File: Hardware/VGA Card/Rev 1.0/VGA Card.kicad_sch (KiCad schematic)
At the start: 25 parts, among them J1 Conn_02x08_Odd_Even, J2 6502 Card Edge, J3 DE15_Receptacle_HighDensity_M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, Q1 BSS138, U1 TXS0108EPW, U2 74HC138, U3 TXS0108EPW, U4 Raspberry Pi Pico

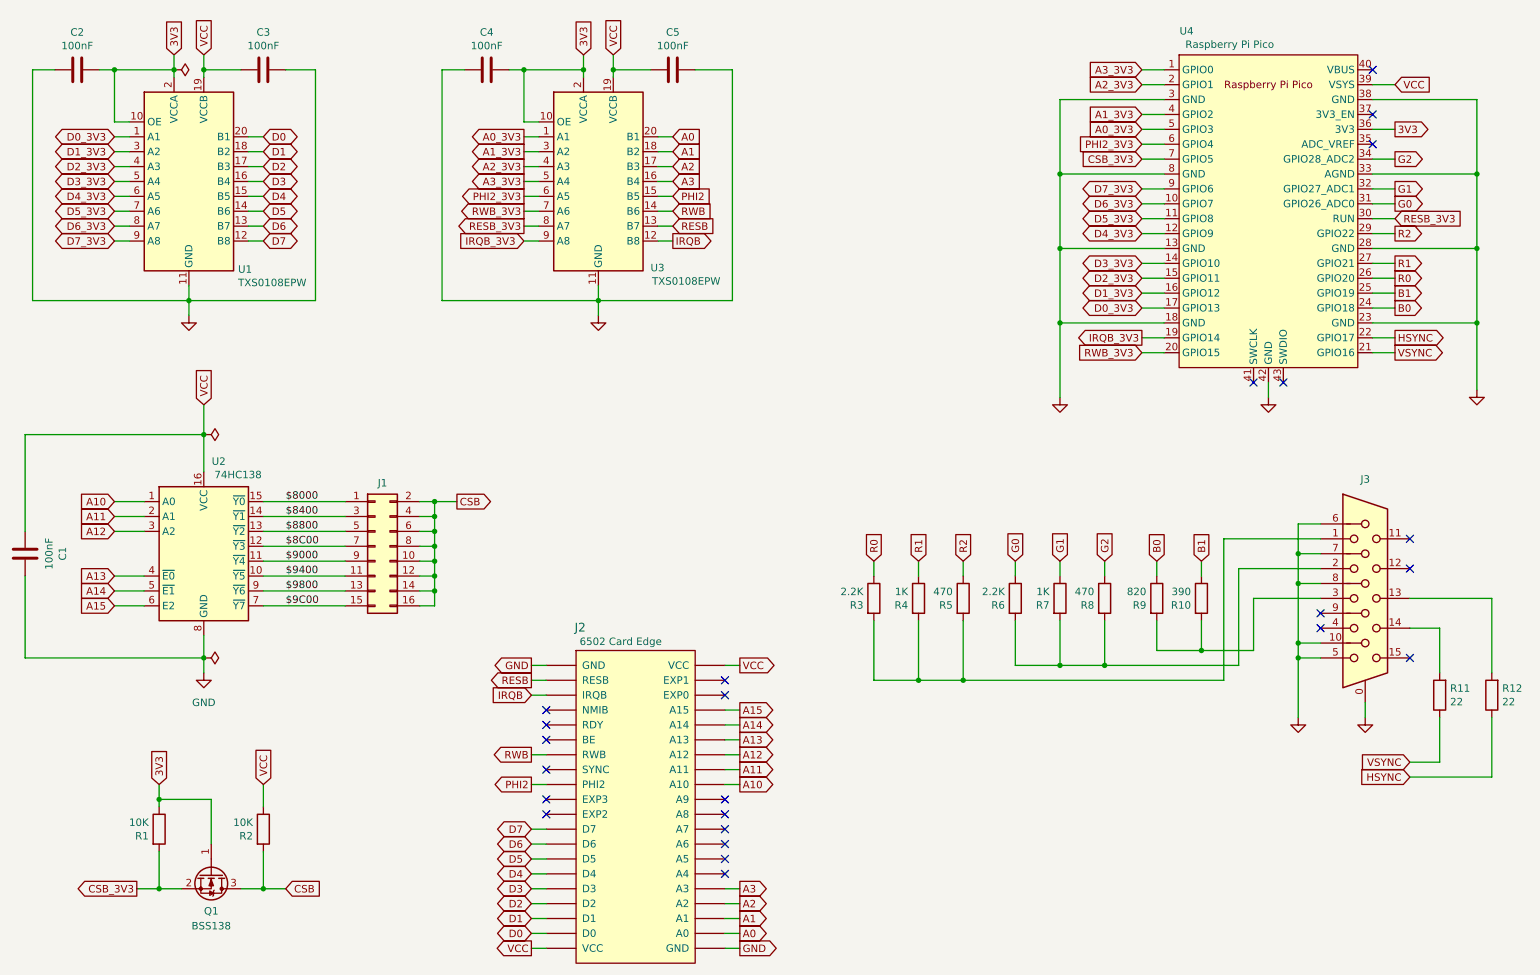
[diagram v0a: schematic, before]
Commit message: Redesign VGA card based on Pico9918A
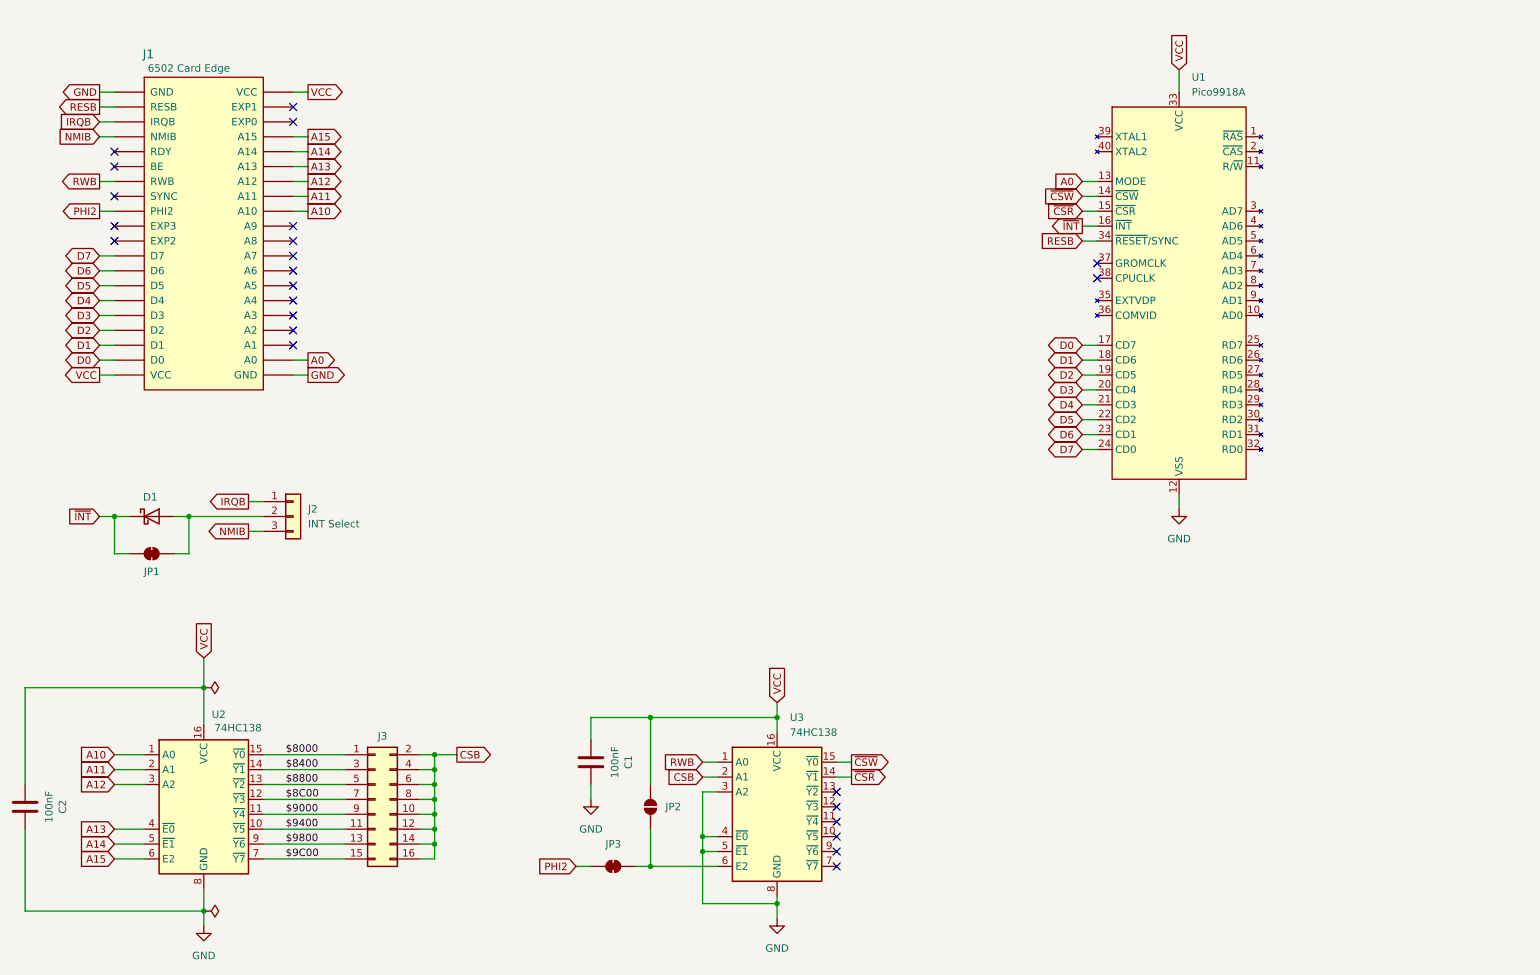
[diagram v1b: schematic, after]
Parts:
- removed C2, C3, C4, C5: 100nF, Capacitor_SMD:C_0805_2012Metric, symbol Device:C
- removed J3: DE15_Receptacle_HighDensity_MountingHoles, Connector_Dsub:DSUB-15-HD_Female_Horizontal_P2.29x1.98mm_EdgePinOffset3.03mm_Housed_MountingHolesOffset4.94mm, symbol Connector:DE15_Receptacle_HighDensity_MountingHoles
- removed Q1: BSS138, Package_TO_SOT_SMD:SOT-23, symbol Transistor_FET:BSS138
- removed R1, R2: 10K, Resistor_SMD:R_0805_2012Metric, symbol Device:R
- removed R10: 390, Resistor_SMD:R_0805_2012Metric, symbol Device:R
- removed R11, R12: 22, Resistor_SMD:R_0805_2012Metric, symbol Device:R
- removed R3, R6: 2.2K, Resistor_SMD:R_0805_2012Metric, symbol Device:R
- removed R4, R7: 1K, Resistor_SMD:R_0805_2012Metric, symbol Device:R
- removed R5, R8: 470, Resistor_SMD:R_0805_2012Metric, symbol Device:R
- removed R9: 820, Resistor_SMD:R_0805_2012Metric, symbol Device:R
- removed U1, U3: TXS0108EPW, Package_SO:TSSOP-20_4.4x6.5mm_P0.65mm, symbol Logic_LevelTranslator:TXS0108EPW
- removed U4: Raspberry Pi Pico, 6502 Parts:Raspberry Pi Pico, symbol 6502 Parts:Raspberry Pi Pico
- added C1: 100nF, Capacitor_SMD:C_0805_2012Metric, symbol Device:C
- added D1: D_Schottky, Diode_THT:D_DO-35_SOD27_P7.62mm_Horizontal, symbol Device:D_Schottky
- added J2: INT Select, Connector_PinHeader_2.54mm:PinHeader_1x03_P2.54mm_Vertical, symbol Connector_Generic:Conn_01x03
- added JP1, JP3: SolderJumper_2_Bridged, Jumper:SolderJumper-2_P1.3mm_Bridged_RoundedPad1.0x1.5mm, symbol Jumper:SolderJumper_2_Bridged
- added JP2: SolderJumper_2_Open, Jumper:SolderJumper-2_P1.3mm_Open_RoundedPad1.0x1.5mm, symbol Jumper:SolderJumper_2_Open
- added U1: Pico9918A, Package_DIP:DIP-40_W15.24mm_LongPads, symbol 6502 Parts:Pico9918A
- added U3: 74HC138, Package_SO:SOIC-16_3.9x9.9mm_P1.27mm, symbol 74xx:74HC138
- renumbered C1 to C2, J2 to J1, J1 to J3
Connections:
- net A0: now also U1.13 (MODE)
- net CSB: now also U3.2 (A1)
- net D0: now also U1.17 (CD7)
- net D1: now also U1.18 (CD6)
- net D2: now also U1.19 (CD5)
- net D3: now also U1.20 (CD4)
- net D4: now also U1.21 (CD3)
- net D5: now also U1.22 (CD2)
- net D6: now also U1.23 (CD1)
- net D7: now also U1.24 (CD0)
- net GND: now also C1.2, U1.12 (VSS), U3.3 (A2), U3.4 (~{E0}), U3.5 (~{E1}), U3.8 (GND)
- net IRQB: now also J2.1 (Pin_1)
- net PHI2: now also JP3.2 (B)
- net RESB: now also U1.34 (~{RESET}/SYNC)
- net RWB: now also U3.1 (A0)
- net VCC: now also C1.1, JP2.1 (A), U1.33 (VCC), U3.16 (VCC)
- net NMIB: now reaches J1.NMIB
- net NMIB: now also J2.3 (Pin_3)
- net A1: no longer names the net of J1.A1
- net A2: no longer names the net of J1.A2
- net A3: no longer names the net of J1.A3
- new net: D1.2 (A), J2.2 (Pin_2), JP1.2 (B)
- new net: JP2.2 (B), JP3.1 (A), U3.6 (E2)
- new net ~{CSR}: U1.15 (~{CSR}), U3.14 (~{Y1})
- new net ~{CSW}: U1.14 (~{CSW}), U3.15 (~{Y0})
- new net ~{INT}: D1.1 (K), JP1.1 (A), U1.16 (~{INT})
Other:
- moved on the sheet: C2, J1, J3, U2

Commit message: Fixes for production
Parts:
- U1: now left out of the parts list
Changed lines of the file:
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@@
 		(unit 1)
 		(exclude_from_sim no)
-		(in_bom yes)
+		(in_bom no)
 		(on_board yes)
 		(dnp no)

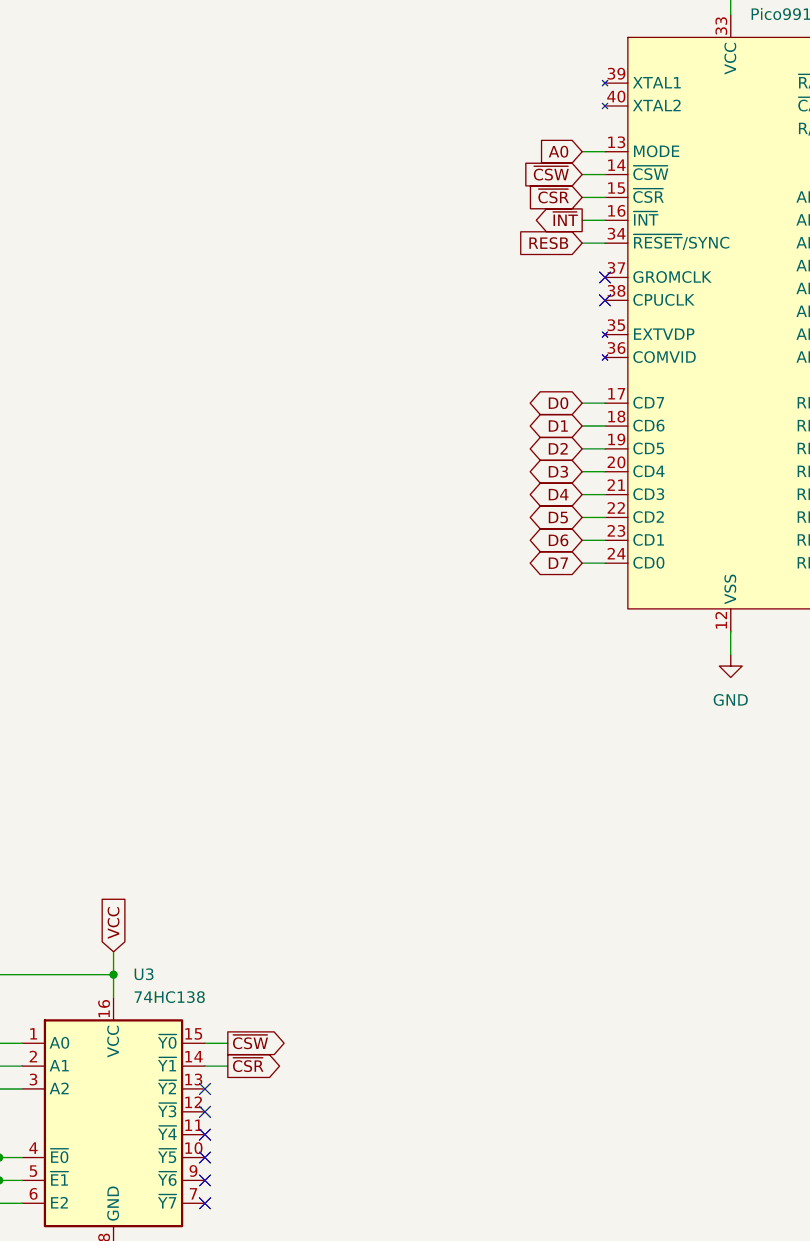
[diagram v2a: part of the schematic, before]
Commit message: Update schematics for pin naming consistency
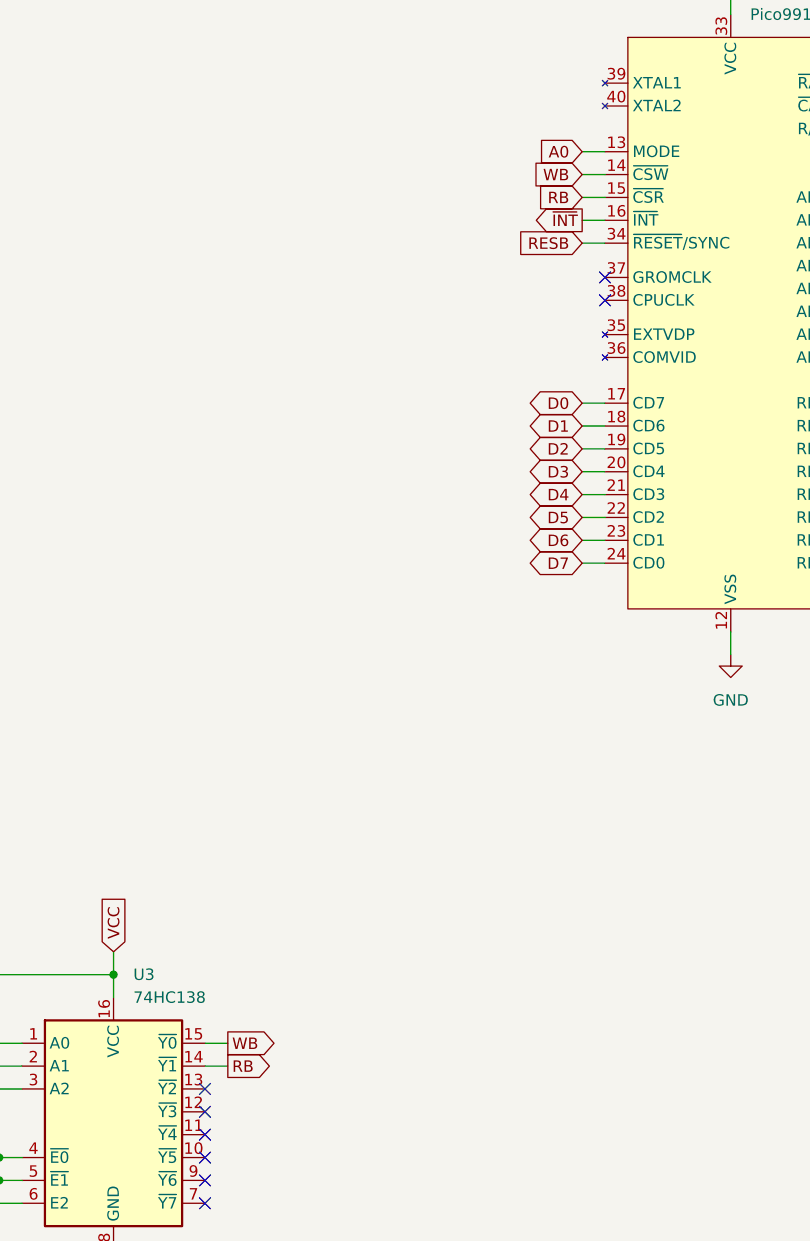
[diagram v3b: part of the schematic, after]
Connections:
- net ~{CSR} renamed RB
- net ~{CSW} renamed WB
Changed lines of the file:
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@@
 		)
 	)
-	(global_label "~{CSW}"
+	(global_label "WB"
 		(shape input)
 		(at 204.47 52.07 180)
@@
 		)
 		(property "Intersheetrefs" "${INTERSHEET_REFS}"
-			(at 197.5539 52.07 0)
+			(at 198.7634 52.07 0)
 			(effects
 				(font
@@
 		)
 	)
-	(global_label "~{CSW}"
+	(global_label "WB"
 		(shape output)
 		(at 165.1 148.59 0)
@@
 		)
 		(property "Intersheetrefs" "${INTERSHEET_REFS}"
-			(at 172.0161 148.59 0)
+			(at 170.8066 148.59 0)
 			(effects
 				(font
@@
 		)
 	)
-	(global_label "~{CSR}"
+	(global_label "RB"
 		(shape input)
 		(at 204.47 54.61 180)
@@
 		)
 		(property "Intersheetrefs" "${INTERSHEET_REFS}"
-			(at 197.7353 54.61 0)
+			(at 198.9448 54.61 0)
 			(effects
 				(font
@@
 		)
 	)
-	(global_label "~{CSR}"
+	(global_label "RB"
 		(shape output)
 		(at 165.1 151.13 0)
@@
 		)
 		(property "Intersheetrefs" "${INTERSHEET_REFS}"
-			(at 171.8347 151.13 0)
-			(effects
-				(font
+			(at 170.6252 151.13 0)
+			(effects
+				(font
